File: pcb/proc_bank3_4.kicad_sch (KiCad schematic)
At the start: 7 parts

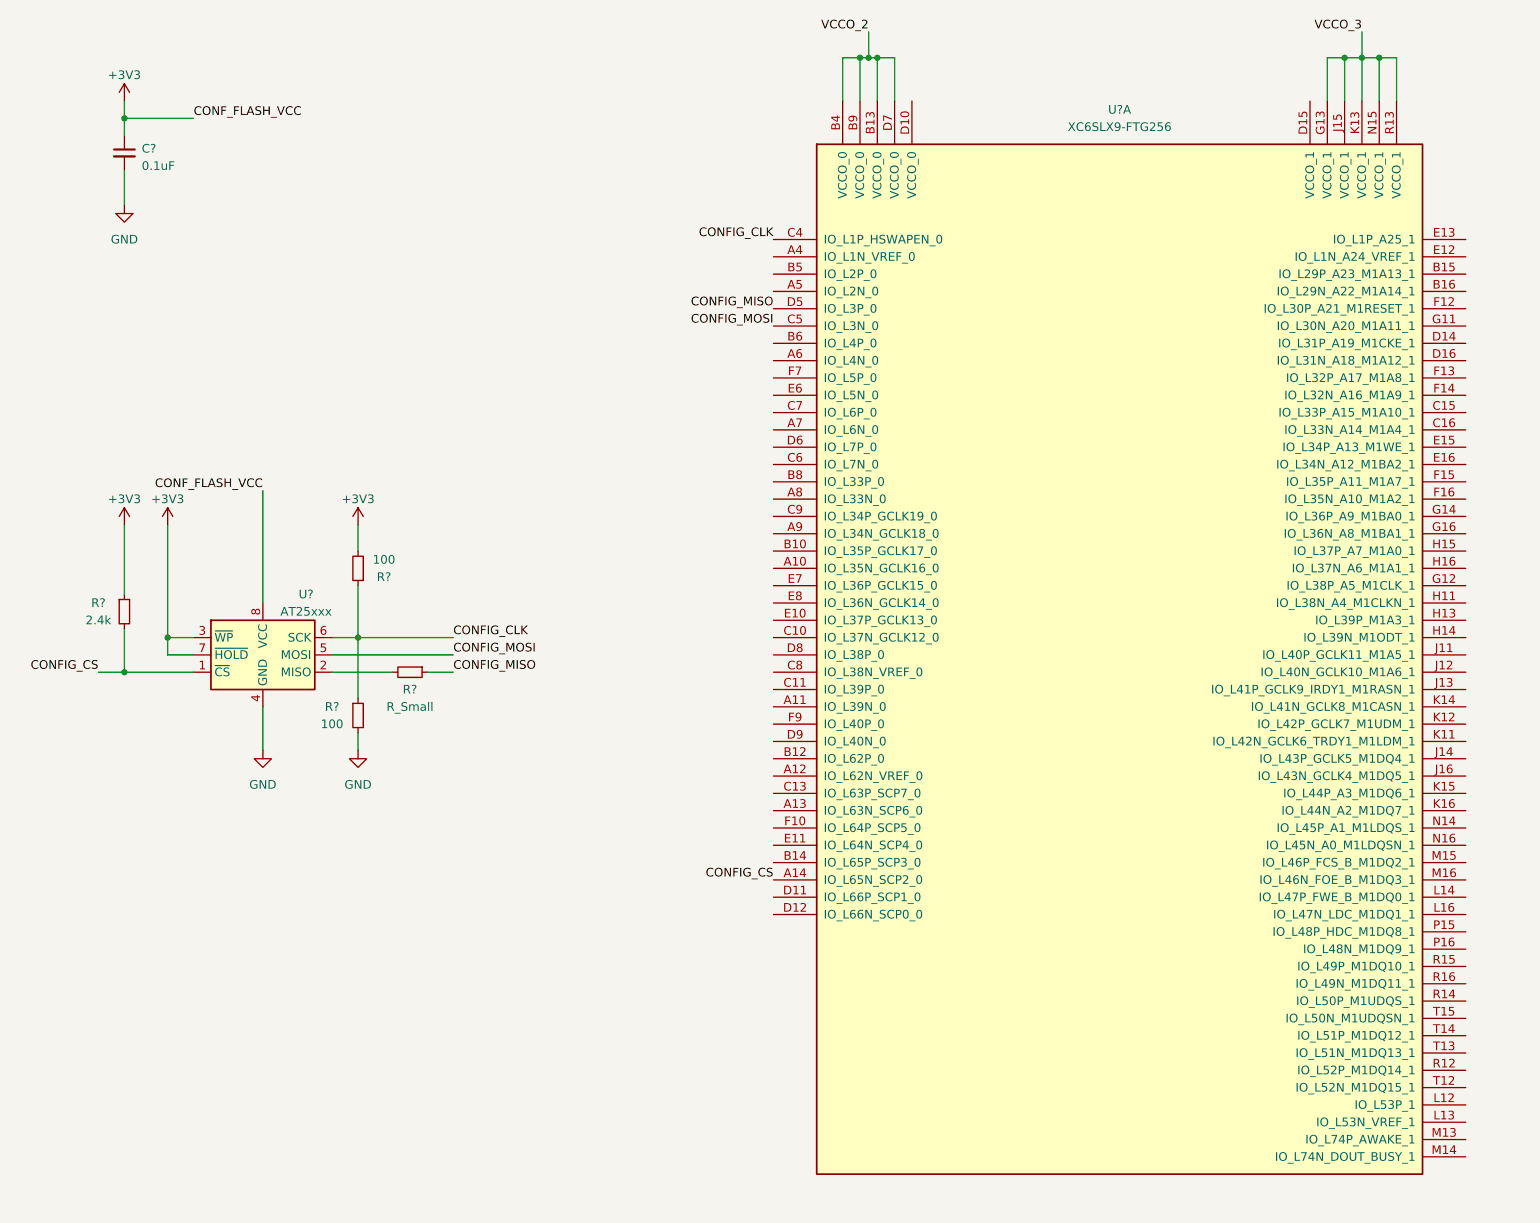
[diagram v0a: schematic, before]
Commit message: add flash memory
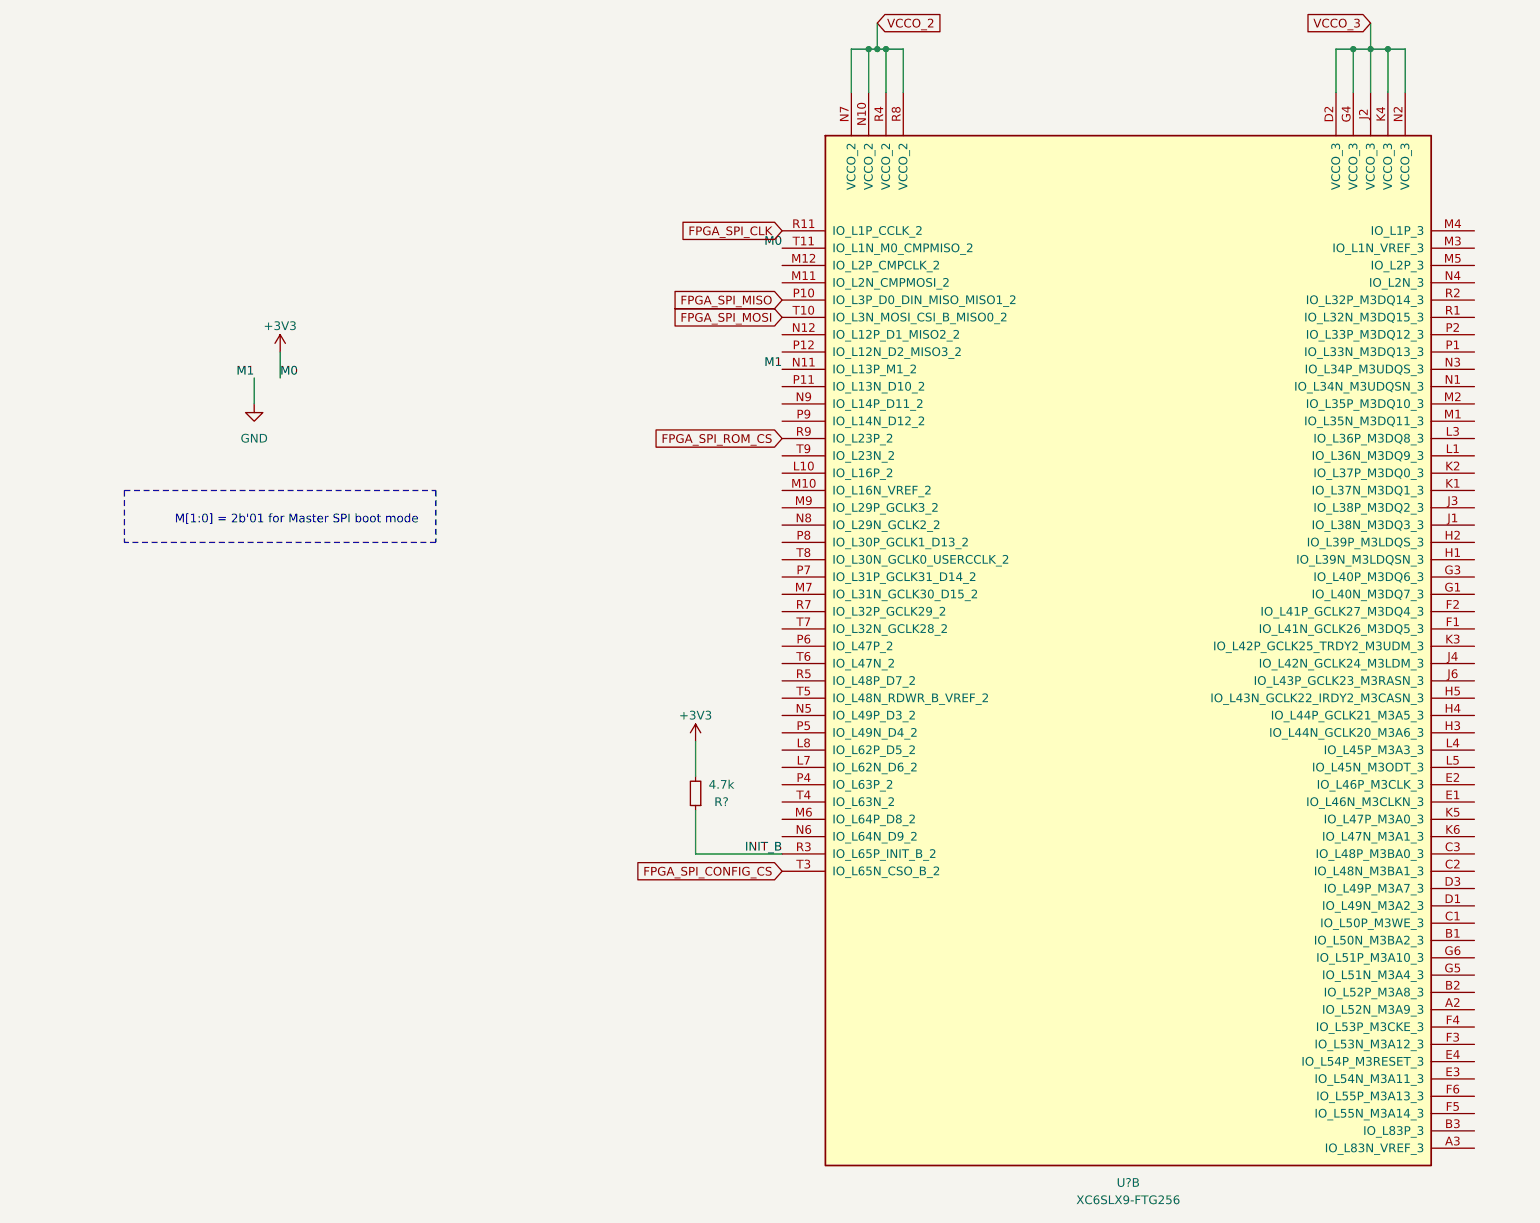
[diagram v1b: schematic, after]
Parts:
- removed C?: 0.1uF, symbol Device:C_Small
- removed R?: R_Small, symbol Device:R_Small
- removed R? (x2): 100, symbol Device:R_Small
- removed R?: 2.4k, symbol Device:R_Small
- removed U?: AT25xxx, symbol Memory_EEPROM:AT25xxx
- removed U?: XC6SLX9-FTG256, symbol FPGA_Xilinx_Spartan6:XC6SLX9-FTG256
- added R?: 4.7k, symbol Device:R_Small
- added U?: XC6SLX9-FTG256, symbol FPGA_Xilinx_Spartan6:XC6SLX9-FTG256
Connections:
- net +3V3: now also R?.2, U?.T11 (IO_L1N_M0_CMPMISO_2)
- net GND: now also U?.N11 (IO_L13P_M1_2)
- net VCCO_2: now also U?.N10 (VCCO_2), U?.N7 (VCCO_2), U?.R4 (VCCO_2), U?.R8 (VCCO_2)
- net VCCO_3: now also U?.D2 (VCCO_3), U?.G4 (VCCO_3), U?.J2 (VCCO_3), U?.K4 (VCCO_3), U?.N2 (VCCO_3)
- new net FPGA_SPI_CLK: U?.R11 (IO_L1P_CCLK_2)
- new net FPGA_SPI_CONFIG_CS: U?.T3 (IO_L65N_CSO_B_2)
- new net FPGA_SPI_MISO: U?.P10 (IO_L3P_D0_DIN_MISO_MISO1_2)
- new net FPGA_SPI_MOSI: U?.T10 (IO_L3N_MOSI_CSI_B_MISO0_2)
- new net FPGA_SPI_ROM_CS: U?.R9 (IO_L23P_2)
- new net INIT_B: R?.1, U?.R3 (IO_L65P_INIT_B_2)
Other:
- note added: "M[1:0] = 2b'01 for Master SPI boot mode"

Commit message: add the din connector
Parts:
- removed U?: XC6SLX9-FTG256, symbol FPGA_Xilinx_Spartan6:XC6SLX9-FTG256
- added U?: XC6SLX16-FTG256, symbol FPGA_Xilinx_Spartan6:XC6SLX16-FTG256
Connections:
- net +3V3: now also U?.T11 (IO_L1N_M0_CMPMISO_2)
- net FPGA_SPI_CLK: now also U?.R11 (IO_L1P_CCLK_2)
- net FPGA_SPI_CONFIG_CS: now also U?.T3 (IO_L65N_CSO_B_2)
- net FPGA_SPI_MISO: now also U?.P10 (IO_L3P_D0_DIN_MISO_MISO1_2)
- net FPGA_SPI_MOSI: now also U?.T10 (IO_L3N_MOSI_CSI_B_MISO0_2)
- net FPGA_SPI_ROM_CS: now also U?.L10 (IO_L16P_2)
- net GND: now also U?.N11 (IO_L13P_M1_2)
- net INIT_B: now also U?.R3 (IO_L65P_INIT_B_2)
- net VCCO_2: now also U?.N10 (VCCO_2), U?.N7 (VCCO_2), U?.R4 (VCCO_2), U?.R8 (VCCO_2)
- net VCCO_3: now also U?.D2 (VCCO_3), U?.G4 (VCCO_3), U?.J2 (VCCO_3), U?.K4 (VCCO_3), U?.N2 (VCCO_3)
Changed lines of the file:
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@@
     (pin "2")
   )
-  (symbol (lib_id "FPGA_Xilinx_Spartan6:XC6SLX9-FTG256") (at 185.42 114.3 0) (unit 2)
+  (symbol (lib_id "FPGA_Xilinx_Spartan6:XC6SLX16-FTG256") (at 185.42 114.3 0) (unit 2)
     (in_bom yes) (on_board yes) (fields_autoplaced)
     (property "Reference" "U?" (id 0) (at 185.42 195.58 0))
-    (property "Value" "XC6SLX9-FTG256" (id 1) (at 185.42 198.12 0))
+    (property "Value" "XC6SLX16-FTG256" (id 1) (at 185.42 198.12 0))
     (property "Footprint" "" (id 2) (at 185.42 114.3 0)
       (effects (font (size 1.27 1.27)) hide)

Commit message: start associating footprints
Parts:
- gave numbers to parts that had none: 2
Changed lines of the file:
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@@
   (symbol (lib_id "power:+3V3") (at 60.96 73.66 0) (mirror y) (unit 1)
     (in_bom yes) (on_board yes) (fields_autoplaced)
-    (property "Reference" "#PWR?" (id 0) (at 60.96 77.47 0)
+    (property "Reference" "#PWR087" (id 0) (at 60.96 77.47 0)
       (effects (font (size 1.27 1.27)) hide)
     )
@@
   (symbol (lib_id "power:+3V3") (at 121.92 130.81 0) (unit 1)
     (in_bom yes) (on_board yes) (fields_autoplaced)
-    (property "Reference" "#PWR?" (id 0) (at 121.92 134.62 0)
+    (property "Reference" "#PWR089" (id 0) (at 121.92 134.62 0)
       (effects (font (size 1.27 1.27)) hide)
     )
@@
   (symbol (lib_id "power:GND") (at 57.15 81.28 0) (mirror y) (unit 1)
     (in_bom yes) (on_board yes) (fields_autoplaced)
-    (property "Reference" "#PWR?" (id 0) (at 57.15 87.63 0)
+    (property "Reference" "#PWR088" (id 0) (at 57.15 87.63 0)
       (effects (font (size 1.27 1.27)) hide)
     )
@@
   (symbol (lib_id "Device:R_Small") (at 121.92 138.43 180) (unit 1)
     (in_bom yes) (on_board yes)
-    (property "Reference" "R?" (id 0) (at 125.73 139.7 0))
+    (property "Reference" "R32" (id 0) (at 125.73 139.7 0))
     (property "Value" "4.7k" (id 1) (at 125.73 137.16 0))
     (property "Footprint" "" (id 2) (at 121.92 138.43 0)
@@
   (symbol (lib_id "FPGA_Xilinx_Spartan6:XC6SLX16-FTG256") (at 185.42 114.3 0) (unit 2)
     (in_bom yes) (on_board yes) (fields_autoplaced)
-    (property "Reference" "U?" (id 0) (at 185.42 195.58 0))
+    (property "Reference" "U1" (id 0) (at 185.42 195.58 0))
     (property "Value" "XC6SLX16-FTG256" (id 1) (at 185.42 198.12 0))
     (property "Footprint" "" (id 2) (at 185.42 114.3 0)

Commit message: add tps541620 footprint
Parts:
- R32: footprint (none) -> Resistor_SMD:R_0402_1005Metric
- U1: footprint (none) -> Package_BGA:Xilinx_FTG256
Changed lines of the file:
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@@
     (property "Reference" "R32" (id 0) (at 125.73 139.7 0))
     (property "Value" "4.7k" (id 1) (at 125.73 137.16 0))
-    (property "Footprint" "" (id 2) (at 121.92 138.43 0)
+    (property "Footprint" "Resistor_SMD:R_0402_1005Metric" (id 2) (at 121.92 138.43 0)
       (effects (font (size 1.27 1.27)) hide)
     )
@@
     (property "Reference" "U1" (id 0) (at 185.42 195.58 0))
     (property "Value" "XC6SLX16-FTG256" (id 1) (at 185.42 198.12 0))
-    (property "Footprint" "" (id 2) (at 185.42 114.3 0)
+    (property "Footprint" "Package_BGA:Xilinx_FTG256" (id 2) (at 185.42 114.3 0)
       (effects (font (size 1.27 1.27)) hide)
     )

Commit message: add the front led glue logic
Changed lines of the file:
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@@
+    (stroke (width 0) (type solid) (color 0 0 0 0))
+  )
+  (wire (pts (xy 127 149.86) (xy 134.62 149.86))
     (stroke (width 0) (type solid) (color 0 0 0 0))
   )
@@
     (effects (font (size 1.27 1.27)) (justify right bottom))
   )
+  (global_label "FPGA_SPI_CONFIG_CS" (shape input) (at 127 149.86 180) (fields_autoplaced)
+    (effects (font (size 1.27 1.27)) (justify right))
+    (property "Intersheet References" "${INTERSHEET_REFS}" (id 0) (at 104.5088 149.7806 0)
+      (effects (font (size 1.27 1.27)) (justify right) hide)
+    )
+  )
   (global_label "FPGA_SPI_CLK" (shape input) (at 134.62 55.88 180) (fields_autoplaced)
     (effects (font (size 1.27 1.27)) (justify right))
@@
       (effects (font (size 1.27 1.27)) (justify right) hide)
     )
-  )
-  (global_label "FPGA_SPI_CONFIG_CS" (shape input) (at 134.62 149.86 180) (fields_autoplaced)
-    (effects (font (size 1.27 1.27)) (justify right))
-    (property "Intersheet References" "${INTERSHEET_REFS}" (id 0) (at 112.1288 149.7806 0)
-      (effects (font (size 1.27 1.27)) (justify right) hide)
-    )

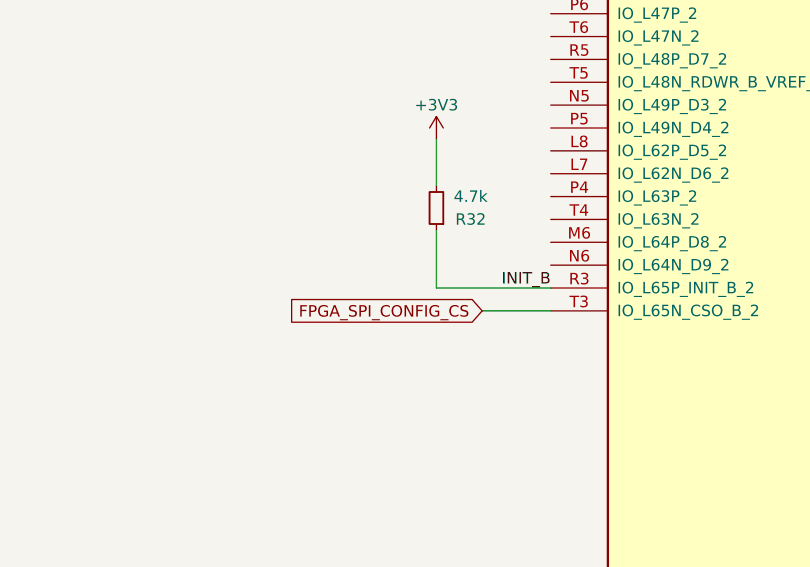
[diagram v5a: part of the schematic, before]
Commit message: add the led blinking logic
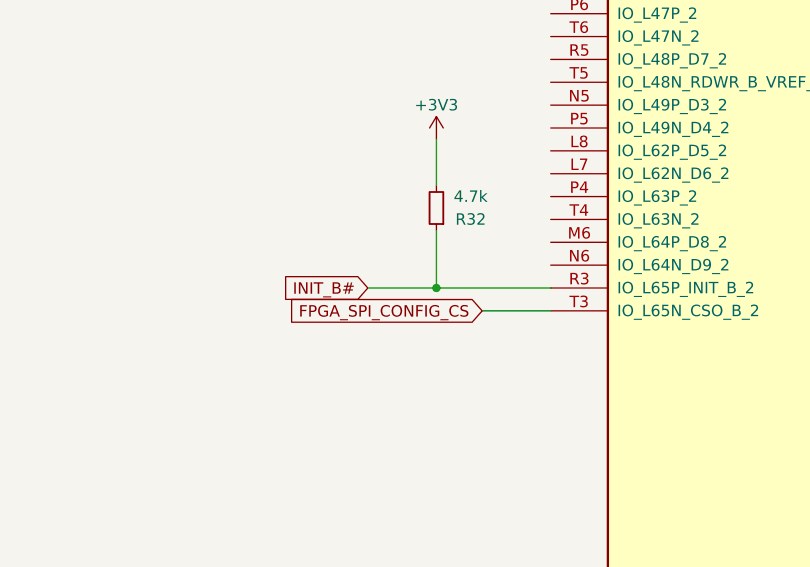
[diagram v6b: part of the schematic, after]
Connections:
- net INIT_B renamed INIT_B#
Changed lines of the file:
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@@
 (kicad_sch (version 20210126) (generator eeschema)
   (paper "User" 280.01 240.005)
+  (junction (at 121.92 147.32) (diameter 0.9144) (color 0 0 0 0))
   (junction (at 147.32 29.21) (diameter 0.9144) (color 0 0 0 0))
   (junction (at 148.59 29.21) (diameter 0.9144) (color 0 0 0 0))
@@
   )
   (wire (pts (xy 60.96 73.66) (xy 60.96 77.47))
+    (stroke (width 0) (type solid) (color 0 0 0 0))
+  )
+  (wire (pts (xy 114.3 147.32) (xy 121.92 147.32))
     (stroke (width 0) (type solid) (color 0 0 0 0))
   )
@@
     (effects (font (size 1.27 1.27)) (justify right bottom))
   )
-  (label "INIT_B" (at 134.62 147.32 180)
-    (effects (font (size 1.27 1.27)) (justify right bottom))
+  (global_label "INIT_B#" (shape input) (at 114.3 147.32 180) (fields_autoplaced)
+    (effects (font (size 1.27 1.27)) (justify right))
+    (property "Intersheet References" "${INTERSHEET_REFS}" (id 0) (at 104.8717 147.2406 0)
+      (effects (font (size 1.27 1.27)) (justify right) hide)
+    )
   )
   (global_label "FPGA_SPI_CONFIG_CS" (shape input) (at 127 149.86 180) (fields_autoplaced)
